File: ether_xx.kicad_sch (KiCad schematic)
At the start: 2 parts, among them U2 LAN8710A, U3 LAN8710A

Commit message: Add missing file and update .pro
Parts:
- added C1: 1nF, Capacitor_SMD:C_1206_3216Metric, symbol karl-atomic-basic:KC1206_1nF_2kV
- added FL1, FL2: Choke_CommonMode_FerriteCore_1234, symbol Filter:Choke_CommonMode_FerriteCore_1234
- added FL3: Choke_CommonMode_FerriteCore_1324, symbol Filter:Choke_CommonMode_FerriteCore_1324
- added J1, J2: RJ45_LED_Shielded, symbol Connector:RJ45_LED_Shielded
- added R1, R2, R3, R4, R5: 75R, Resistor_SMD:R_0603_1608Metric, symbol karl-atomic-basic:KR0603_75R
- added TR1: TRANSF5, symbol Transformer:TRANSF5
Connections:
- new net: C1.1, R2.2, R3.2
- new net: J1.4, J1.5, R2.1
- new net: J1.6, J1.7, R3.1

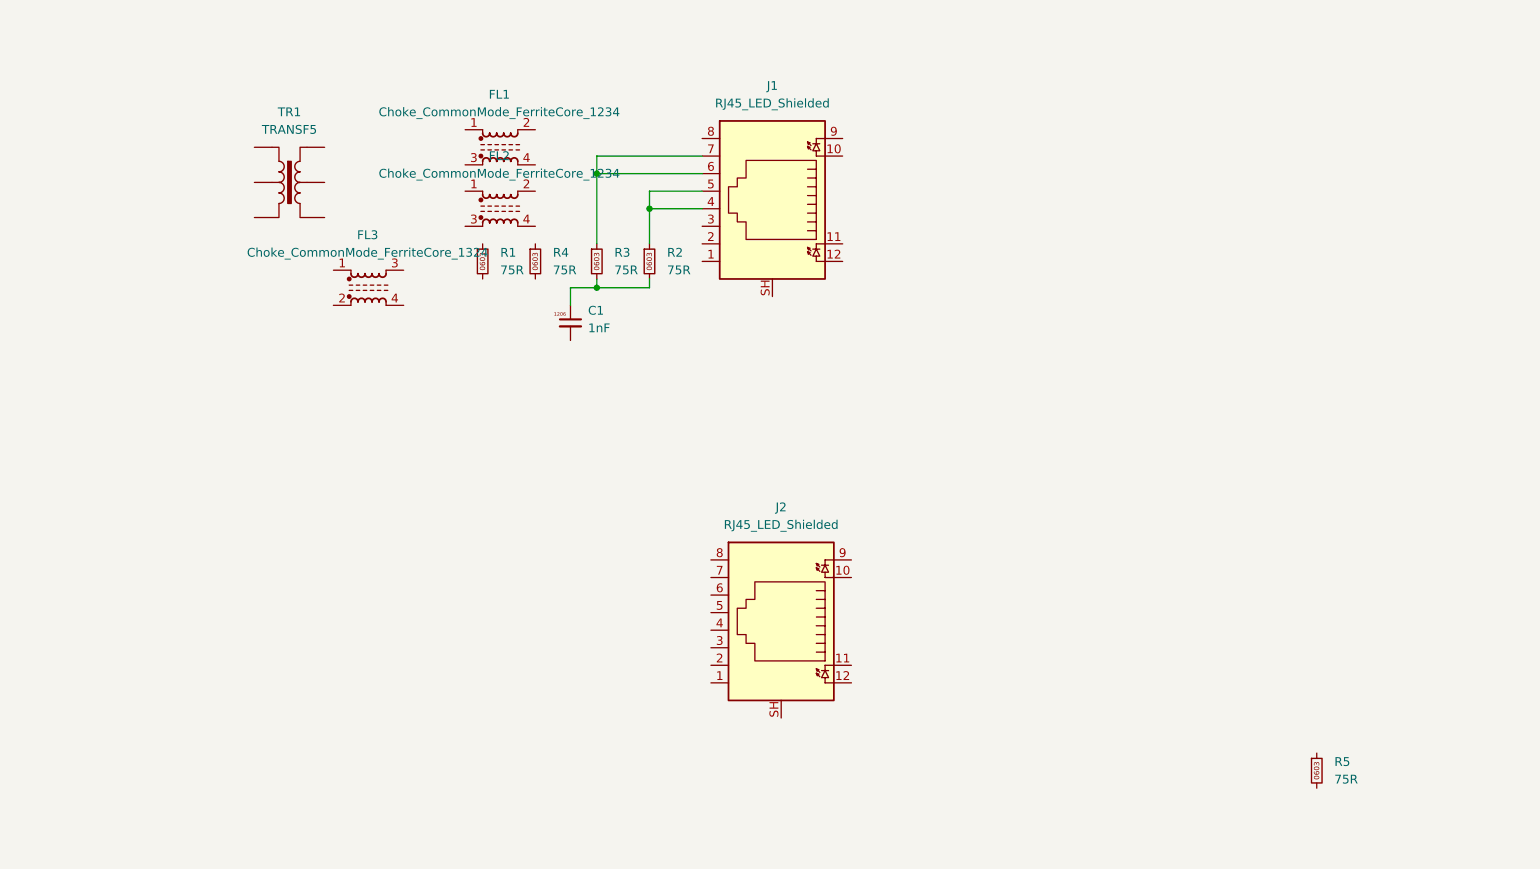
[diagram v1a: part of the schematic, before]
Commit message: sketching continues
You cannot do MII on F100 package, so don't even try on the F144,
there's no saving vs the E196.

Start stuffing in what else you'd actually need for this.  Give it a pi
interface to use as a daughterboard, usb to use standalone, jbt marel
can to use there,

always underestimate just how much _stuff_ there is to do though...
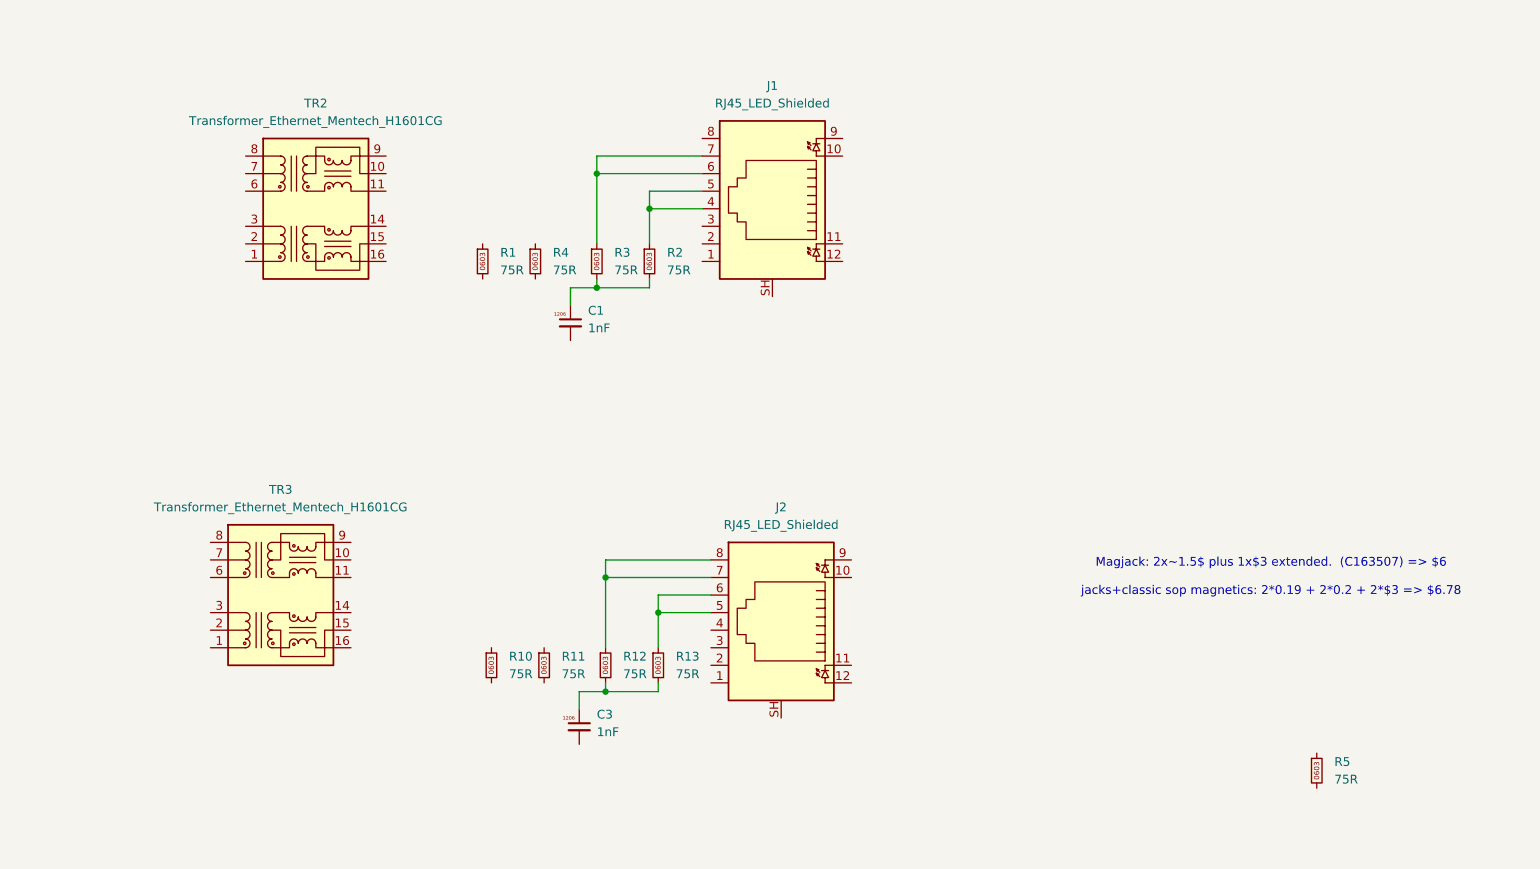
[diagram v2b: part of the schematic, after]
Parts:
- removed FL1, FL2: Choke_CommonMode_FerriteCore_1234, symbol Filter:Choke_CommonMode_FerriteCore_1234
- removed FL3: Choke_CommonMode_FerriteCore_1324, symbol Filter:Choke_CommonMode_FerriteCore_1324
- removed TR1: TRANSF5, symbol Transformer:TRANSF5
- added C3: 1nF, Capacitor_SMD:C_1206_3216Metric, symbol karl-atomic-basic:KC1206_1nF_2kV
- added R10, R11, R12, R13: 75R, Resistor_SMD:R_0603_1608Metric, symbol karl-atomic-basic:KR0603_75R
- added TR2, TR3: Transformer_Ethernet_Mentech_H1601CG, et-parts:Transformer_Ethernet_Dongguan-MentechH1651CG_SO-12_7.1x12.7mm, symbol etactica-parts:Transformer_Ethernet_Mentech_H1601CG
- U3: LCSC # C46185 -> (none); LCSC Part # (none) -> C46185
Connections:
- net at J2.5: now also J2.6, R13.1
- net at J2.7: now also J2.8, R12.1
- new net: C3.1, R12.2, R13.2
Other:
- note added: "Magjack: 2x~1.5$ plus 1x$3 extended. (C163507) => $6 jacks+classic sop magnetics: 2*0.19 + 2*0.2 + 2*$3 => $6.78"

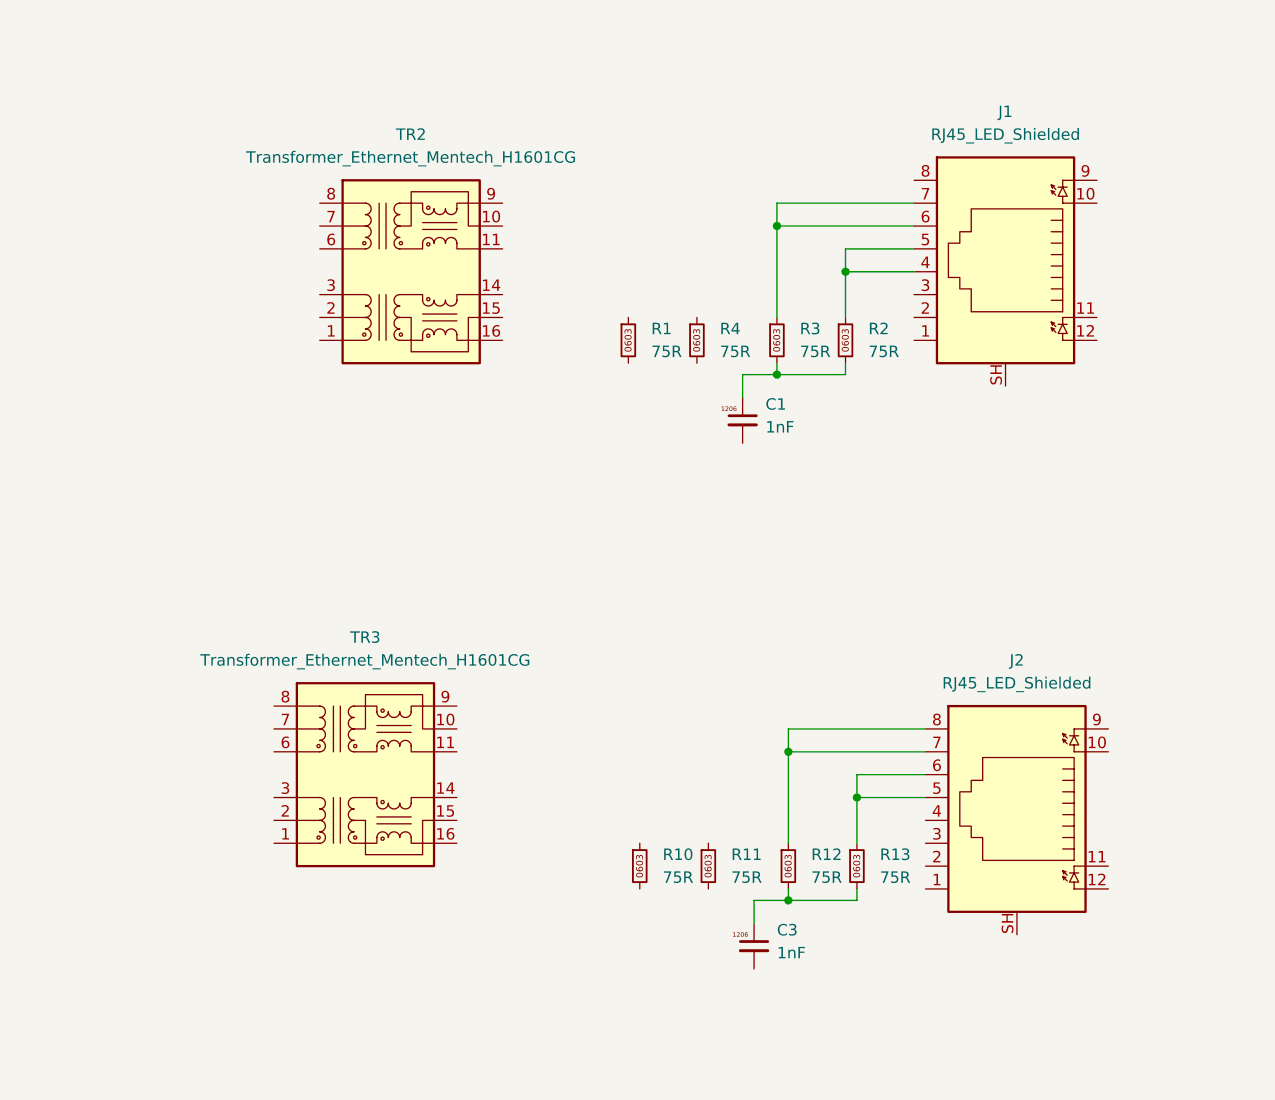
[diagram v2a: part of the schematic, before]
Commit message: finish the tism on magnetics.
jsut use H110X symbol numbering and any H110x footprint, they're all the
same.
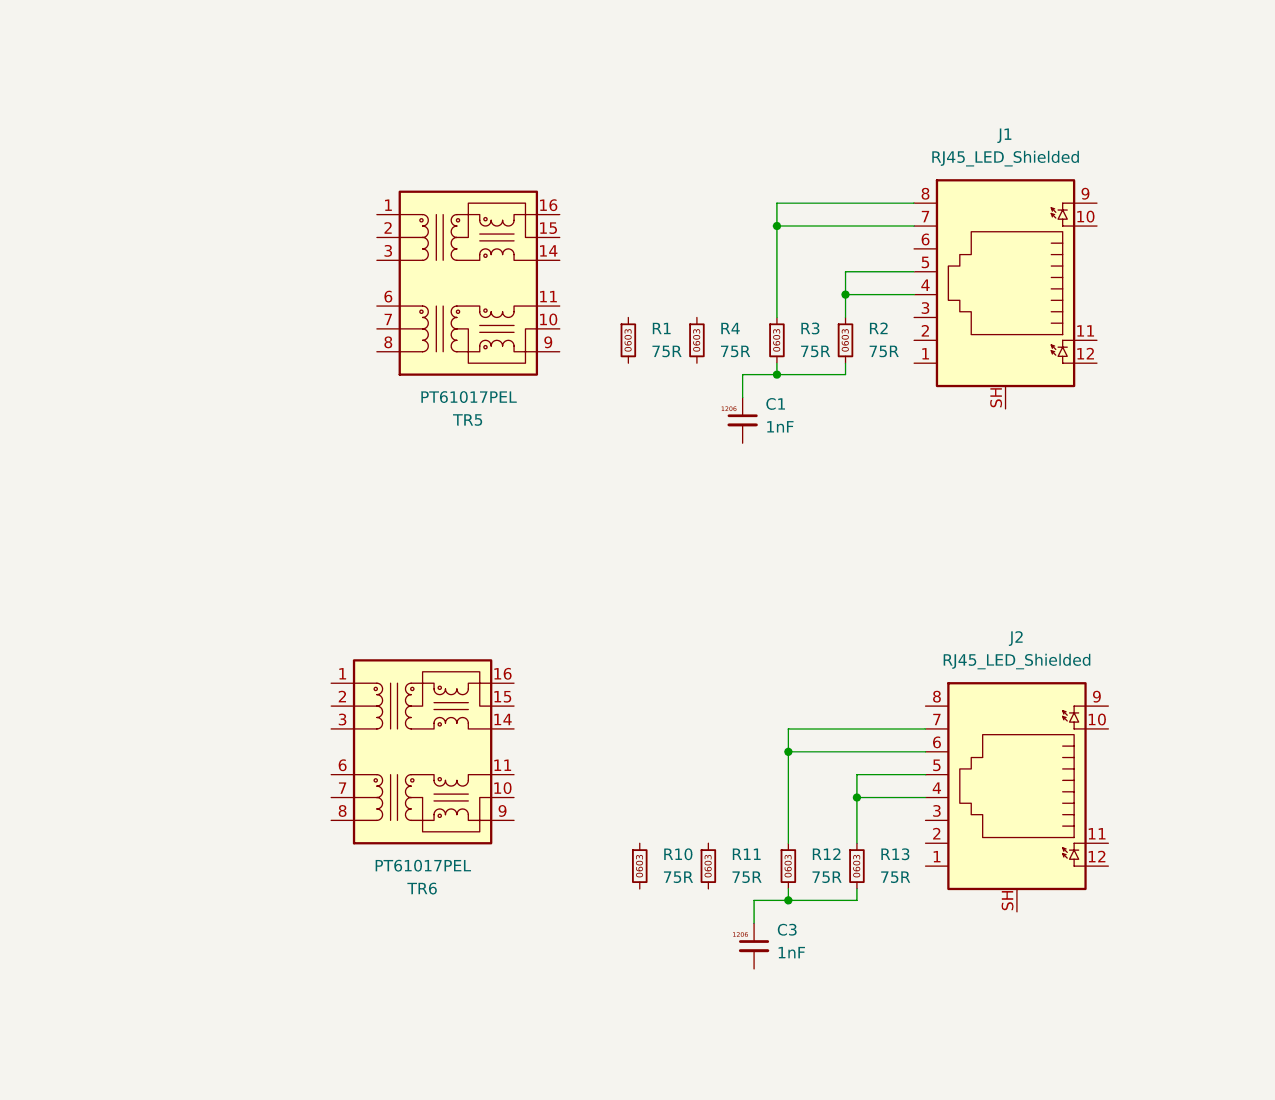
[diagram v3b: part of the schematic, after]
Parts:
- removed TR2, TR3: Transformer_Ethernet_Mentech_H1601CG, et-parts:Transformer_Ethernet_Dongguan-MentechH1651CG_SO-12_7.1x12.7mm, symbol etactica-parts:Transformer_Ethernet_Mentech_H1601CG
- added TR5, TR6: PT61017PEL, Transformer_SMD:Transformer_Ethernet_Bourns_PT61017PEL, symbol Transformer:PT61017PEL
- J1: footprint (none) -> Connector_RJ:RJ45_Amphenol_RJHSE538X; LCSC Part # (none) -> C7501824; LCSC# C7501824 -> (none); MPN (none) -> HC-WK88-H16-DB
- J2: footprint (none) -> Connector_RJ:RJ45_Amphenol_RJHSE538X; LCSC Part # (none) -> C7501824; MPN (none) -> HC-WK88-H16-DB
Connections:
- net at J1.7, R3.1: now also J1.8; no longer J1.6
- net at J2.5, R13.1: now also J2.4; no longer J2.6
- net at J2.7, R12.1: now also J2.6; no longer J2.8
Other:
- moved on the sheet: J1
